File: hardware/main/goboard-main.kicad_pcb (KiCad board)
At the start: 2 copper layers, 312.7 x 138.4 mm, 152 parts, among them J1 USB_C_Receptacle_USB2.0, J2 Conn_02x05_Top_Bottom, J3 Conn_01x01, SW1 Esc, SW10 a, SW12 Fn, SW13 F2, SW14 2, SW15 w, SW16 s, SW17 z, SW18 Tux, SW19 F3, SW2 F1, SW20 3, SW21 e, SW22 d, SW23 c, SW24 Alt, SW25 F4, SW26 4, SW27 r, SW28 f, SW29 v, SW3 tilde, SW31 F5, SW32 5, SW33 t, SW34 g, SW35 b, SW36 F6, SW37 6, SW38 y, SW39 h, SW4 Tab, SW40 n, SW41 F7, SW42 7, SW43 u, SW44 j, SW45 m, SW46 Space, SW47 F8, SW48 8, SW49 i, SW5 Caps Lock, SW50 k, SW51 ,, SW52 F9, SW53 9, SW54 o, SW55 l, SW56 ., SW57 F10, SW58 0, SW59 p, SW6 Shift, SW60 ;, SW61 /, SW62 Alt Gr, SW63 F11, SW64 -, SW65 [, SW66 ', SW67 Menu, SW68 F12, SW69 =, SW7 Ctrl, SW70 ], SW71 \, SW72 Shift, SW73 Ctrl, SW74 Print, SW75 Backspace, SW76 Enter, SW77 Left, SW78 Scroll Lock, SW79 Up, SW8 1, SW80 Down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

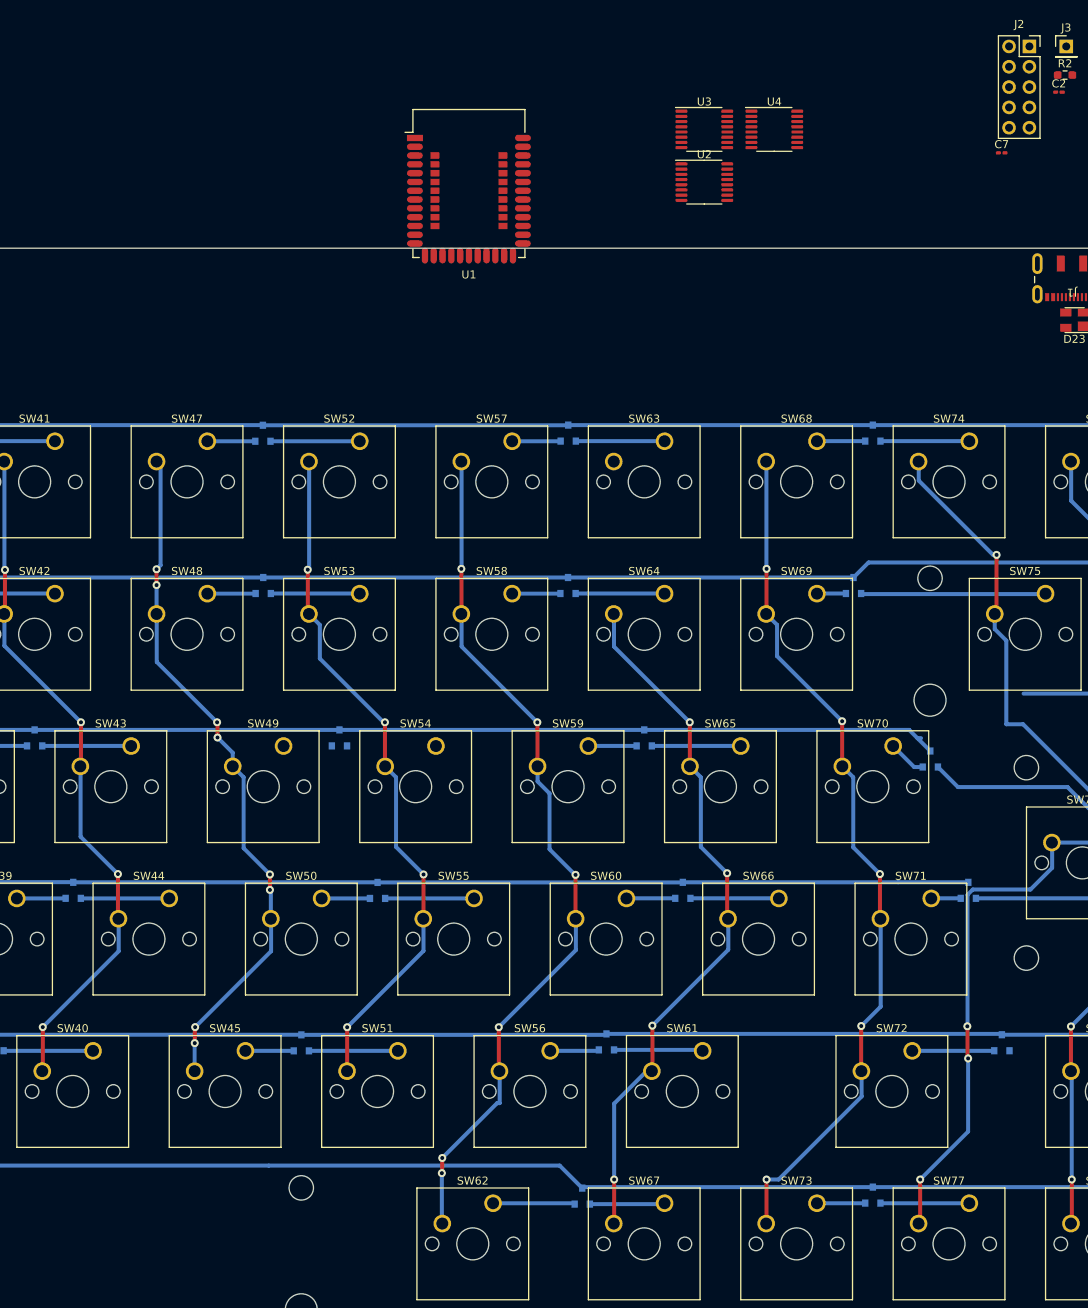
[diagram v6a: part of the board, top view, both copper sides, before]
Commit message: Add specialized connector for the programming port
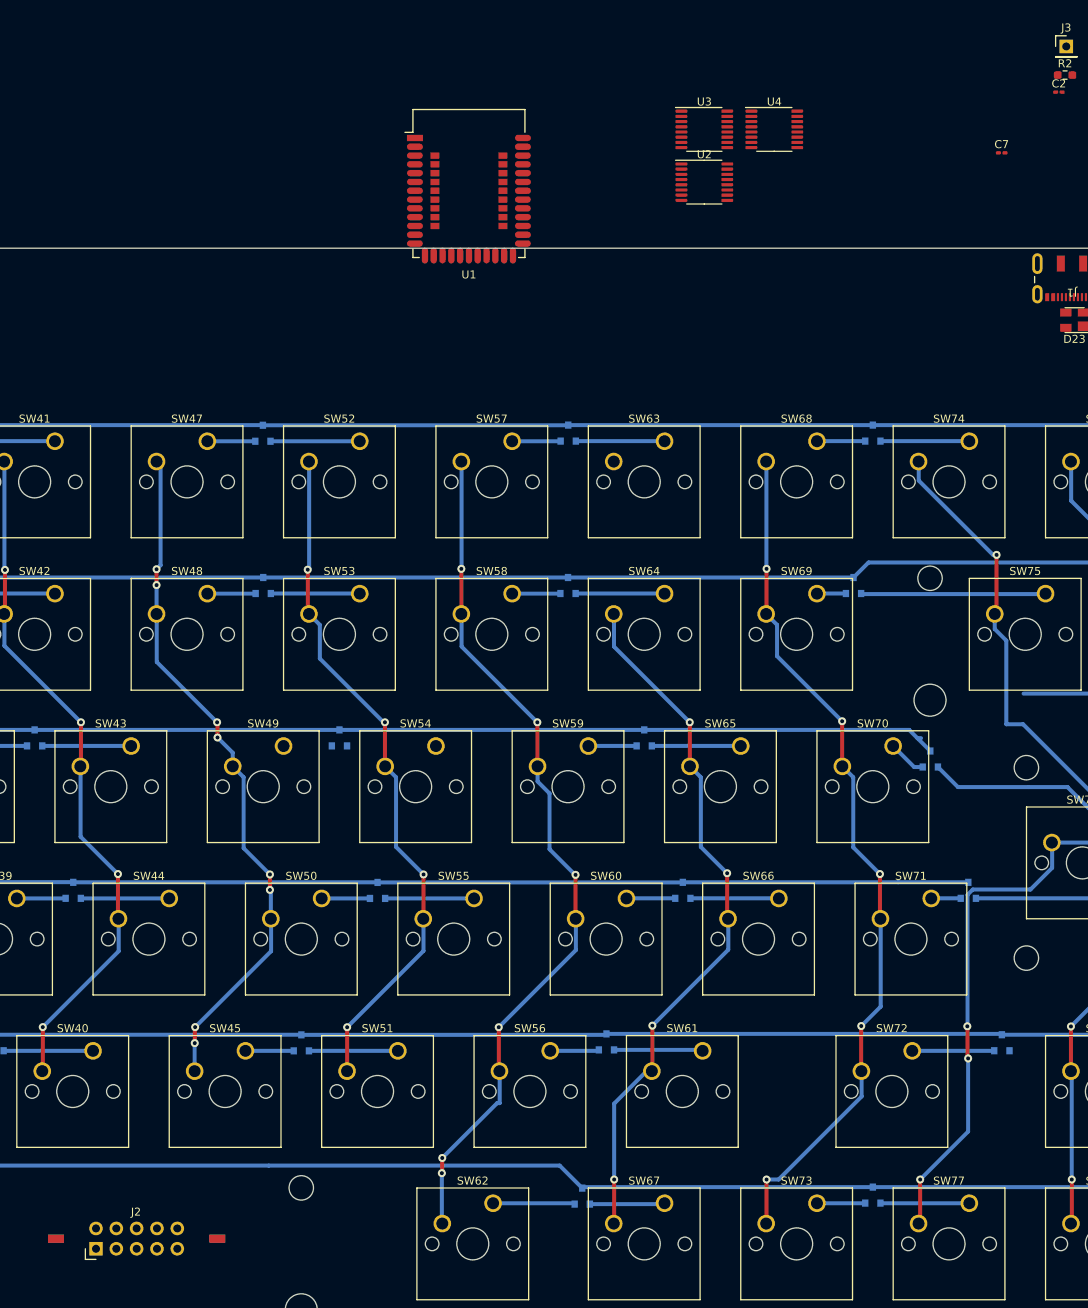
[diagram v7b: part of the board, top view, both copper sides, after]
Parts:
- J2: footprint Connector_PinSocket_2.54mm:PinSocket_2x05_P2.54mm_Vertical -> footprints:programming_port_st_link_clone
- moved J2 190.3 mm to (189.5, 174.7)
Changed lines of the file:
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@@
     )
   )
-  (footprint "Connector_PinSocket_2.54mm:PinSocket_2x05_P2.54mm_Vertical" (layer "F.Cu")
-    (at 306.1308 24.437)
-    (descr "Through hole straight socket strip, 2x05, 2.54mm pitch, double cols (from Kicad 4.0.7), script generated")
-    (tags "Through hole socket strip THT 2x05 2.54mm double row")
+  (footprint "footprints:programming_port_st_link_clone" (layer "F.Cu")
+    (at 189.4586 174.7266)
+    (descr "Through hole straight pin header, 2x05, 2.54mm pitch, double rows")
+    (tags "Through hole pin header THT 2x05 2.54mm double row")
     (property "Dateiname Blatt" "goboard-main.kicad_sch")
     (property "Schaltplanname" "")
     (attr through_hole)
-    (fp_text reference "J2" (at -1.27 -2.77) (layer "F.SilkS")
+    (fp_text reference "J2" (at 5 -4.6 180) (layer "F.SilkS")
       (effects (font (size 1 1) (thickness 0.15)))
     )
-    (fp_text value "Conn_02x05_Top_Bottom" (at -1.27 12.93) (layer "F.Fab")
+    (fp_text value "Conn_02x05_Top_Bottom" (at 5.1 2.1) (layer "F.Fab")
       (effects (font (size 1 1) (thickness 0.15)))
     )
-    (fp_text user "${REFERENCE}" (at -1.27 5.08 90) (layer "F.Fab")
+    (fp_text user "${REFERENCE}" (at 5.08 -1.27 180) (layer "F.Fab")
       (effects (font (size 1 1) (thickness 0.15)))
     )
-    (fp_line (start 0 -1.33) (end 1.33 -1.33) (layer "F.SilkS") (width 0.12))
-    (fp_line (start 1.33 -1.33) (end 1.33 0) (layer "F.SilkS") (width 0.12))
-    (fp_line (start -3.87 -1.33) (end -1.27 -1.33) (layer "F.SilkS") (width 0.12))
-    (fp_line (start 1.33 1.27) (end 1.33 11.49) (layer "F.SilkS") (width 0.12))
-    (fp_line (start -1.27 1.27) (end 1.33 1.27) (layer "F.SilkS") (width 0.12))
-    (fp_line (start -3.87 -1.33) (end -3.87 11.49) (layer "F.SilkS") (width 0.12))
-    (fp_line (start -1.27 -1.33) (end -1.27 1.27) (layer "F.SilkS") (width 0.12))
-    (fp_line (start -3.87 11.49) (end 1.33 11.49) (layer "F.SilkS") (width 0.12))
-    (fp_line (start 1.76 11.9) (end -4.34 11.9) (layer "F.CrtYd") (width 0.05))
-    (fp_line (start 1.76 -1.8) (end 1.76 11.9) (layer "F.CrtYd") (width 0.05))
-    (fp_line (start -4.34 11.9) (end -4.34 -1.8) (layer "F.CrtYd") (width 0.05))
-    (fp_line (start -4.34 -1.8) (end 1.76 -1.8) (layer "F.CrtYd") (width 0.05))
-    (fp_line (start -3.81 -1.27) (end 0.27 -1.27) (layer "F.Fab") (width 0.1))
-    (fp_line (start 1.27 11.43) (end -3.81 11.43) (layer "F.Fab") (width 0.1))
-    (fp_line (start 1.27 -0.27) (end 1.27 11.43) (layer "F.Fab") (width 0.1))
-    (fp_line (start 0.27 -1.27) (end 1.27 -0.27) (layer "F.Fab") (width 0.1))
-    (fp_line (start -3.81 11.43) (end -3.81 -1.27) (layer "F.Fab") (width 0.1))
-    (pad "1" thru_hole rect (at 0 0) (size 1.7 1.7) (drill 1) (layers *.Cu *.Mask)
+    (fp_line (start -1.33 1.33) (end -1.33 0) (layer "F.SilkS") (width 0.12))
+    (fp_line (start 0 1.33) (end -1.33 1.33) (layer "F.SilkS") (width 0.12))
+    (fp_line (start -1.8 -4.35) (end -1.8 -2.5) (layer "F.CrtYd") (width 0.05))
+    (fp_line (start -1.8 0.05) (end -1.8 1.8) (layer "F.CrtYd") (width 0.05))
+    (fp_line (start -1.8 -2.5) (end -6.5 -2.5) (layer "F.CrtYd") (width 0.05))
+    (fp_line (start 16.65 -2.6) (end 11.95 -2.6) (layer "F.CrtYd") (width 0.05))
+    (fp_line (start -6.5 0.05) (end -1.8 0.05) (layer "F.CrtYd") (width 0.05))
+    (fp_line (start 16.65 -0.05) (end 16.65 -2.6) (layer "F.CrtYd") (width 0.05))
+    (fp_line (start 11.95 -4.35) (end -1.8 -4.35) (layer "F.CrtYd") (width 0.05))
+    (fp_line (start -6.5 -2.5) (end -6.5 0.05) (layer "F.CrtYd") (width 0.05))
+    (fp_line (start 11.95 -0.05) (end 16.65 -0.05) (layer "F.CrtYd") (width 0.05))
+    (fp_line (start 11.95 1.8) (end 11.95 -0.05) (layer "F.CrtYd") (width 0.05))
+    (fp_line (start -1.8 1.8) (end 11.95 1.8) (layer "F.CrtYd") (width 0.05))
+    (fp_line (start 11.95 -2.6) (end 11.95 -4.35) (layer "F.CrtYd") (width 0.05))
+    (pad "" smd rect (at 15.16 -1.27 270) (size 1 2) (layers "F.Cu" "F.Paste" "F.Mask"))
+    (pad "" smd rect (at -5 -1.27 90) (size 1 2) (layers "B.Cu" "B.Paste" "B.Mask"))
+    (pad "" np_thru_hole oval (at 12.83 -1.27 270) (size 1 2.5) (drill oval 1 2.5) (layers F&B.Cu *.Mask))
+    (pad "" np_thru_hole oval (at -2.67 -1.27 90) (size 1 2.5) (drill oval 1 2.5) (layers F&B.Cu *.Mask))
+    (pad "" smd rect (at 15.16 -1.27 270) (size 1 2) (layers "B.Cu" "B.Paste" "B.Mask"))
+    (pad "" smd rect (at -5 -1.27 270) (size 1 2) (layers "F.Cu" "F.Paste" "F.Mask"))
+    (pad "1" thru_hole rect (at 0 0 90) (size 1.7 1.7) (drill 1) (layers *.Cu *.Mask)
       (net 37 "/RESET") (pinfunction "Pin_1"))
-    (pad "2" thru_hole oval (at -2.54 0) (size 1.7 1.7) (drill 1) (layers *.Cu *.Mask)
+    (pad "2" thru_hole oval (at 0 -2.54 90) (size 1.7 1.7) (drill 1) (layers *.Cu *.Mask)
       (net 47 "GND") (pinfunction "Pin_2"))
-    (pad "3" thru_hole oval (at 0 2.54) (size 1.7 1.7) (drill 1) (layers *.Cu *.Mask)
+    (pad "3" thru_hole oval (at 2.54 0 90) (size 1.7 1.7) (drill 1) (layers *.Cu *.Mask)
       (net 132 "no_connect_143") (pinfunction "Pin_3"))
-    (pad "4" thru_hole oval (at -2.54 2.54) (size 1.7 1.7) (drill 1) (layers *.Cu *.Mask)
+    (pad "4" thru_hole oval (at 2.54 -2.54 90) (size 1.7 1.7) (drill 1) (layers *.Cu *.Mask)
       (net 31 "VCC") (pinfunction "Pin_4"))
-    (pad "5" thru_hole oval (at 0 5.08) (size 1.7 1.7) (drill 1) (layers *.Cu *.Mask)
+    (pad "5" thru_hole oval (at 5.08 0 90) (size 1.7 1.7) (drill 1) (layers *.Cu *.Mask)
       (net 131 "no_connect_144") (pinfunction "Pin_5"))
-    (pad "6" thru_hole oval (at -2.54 5.08) (size 1.7 1.7) (drill 1) (layers *.Cu *.Mask)
+    (pad "6" thru_hole oval (at 5.08 -2.54 90) (size 1.7 1.7) (drill 1) (layers *.Cu *.Mask)
       (net 130 "/SWDIO") (pinfunction "Pin_6"))
-    (pad "7" thru_hole oval (at 0 7.62) (size 1.7 1.7) (drill 1) (layers *.Cu *.Mask)
+    (pad "7" thru_hole oval (at 7.62 0 90) (size 1.7 1.7) (drill 1) (layers *.Cu *.Mask)
       (net 47 "GND") (pinfunction "Pin_7"))
-    (pad "8" thru_hole oval (at -2.54 7.62) (size 1.7 1.7) (drill 1) (layers *.Cu *.Mask)
+    (pad "8" thru_hole oval (at 7.62 -2.54 90) (size 1.7 1.7) (drill 1) (layers *.Cu *.Mask)
       (net 129 "/SWDCLK") (pinfunction "Pin_8"))
-    (pad "9" thru_hole oval (at 0 10.16) (size 1.7 1.7) (drill 1) (layers *.Cu *.Mask)
+    (pad "9" thru_hole oval (at 10.16 0 90) (size 1.7 1.7) (drill 1) (layers *.Cu *.Mask)
       (net 31 "VCC") (pinfunction "Pin_9"))
-    (pad "10" thru_hole oval (at -2.54 10.16) (size 1.7 1.7) (drill 1) (layers *.Cu *.Mask)
+    (pad "10" thru_hole oval (at 10.16 -2.54 90) (size 1.7 1.7) (drill 1) (layers *.Cu *.Mask)
       (net 128 "no_connect_142") (pinfunction "Pin_10"))
-    (model "${KISYS3DMOD}/Connector_PinSocket_2.54mm.3dshapes/PinSocket_2x05_P2.54mm_Vertical.wrl"
-      (offset (xyz 0 0 0))
-      (scale (xyz 1 1 1))
-      (rotate (xyz 0 0 0))
-    )
   )
   (footprint "footprints:SW_Cherry_MX_1.75u_PCB" (layer "F.Cu")

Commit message: Adapt the layout for another keycap set
The layout is now compatible with this keycap set:
https://hk-gaming.com/collections/keycaps/products/hk-gaming-dye-
sublimation-cherry-profile-thick-pbt-keysets-for-mechanical-keyboard-139
-keys-chalk
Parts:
- removed SW67: Menu, footprints:SW_Cherry_MX_1.00u_PCB
- SW24: footprint footprints:SW_Cherry_MX_1.00u_PCB -> footprints:SW_Cherry_MX_1.25u_PCB
- SW62: footprint footprints:SW_Cherry_MX_1.25u_PCB -> footprints:SW_Cherry_MX_1.50u_PCB
- SW73: footprint footprints:SW_Cherry_MX_1.00u_PCB -> footprints:SW_Cherry_MX_1.50u_PCB
- moved D12 6.74 mm to (107.2, 167.7)
- moved SW62 6.63 mm to (245.3, 171.4)
- moved SW73 6.22 mm to (273.8, 171.4)
- moved SW46 4.49 mm to (171.4, 171.4)
- moved SW24 2.79 mm to (100.0, 171.4)
- moved D32 2.60 mm to (261.8, 132.3)
- moved D38 2.60 mm to (297.5, 132.3)
- moved SW72 2.60 mm to (290.5, 152.4)
- moved C2 2.60 mm to (308.8, 32.6)
- moved C1 2.60 mm to (317.8, 25.4)
- moved D45 2.60 mm to (335.8, 28.4)
- moved D47 2.60 mm to (335.8, 25.8)
- moved D10 2.60 mm to (106.7, 132.4)
- moved D14 2.60 mm to (133.2, 94.1)
- moved D15 2.60 mm to (142.7, 113.3)
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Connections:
- D40 pad 1: Net-(D40-Pad1) -> no_connect_140
- J1 pad A8: no_connect_140 -> no_connect_141
- J1 pad B8: no_connect_141 -> no_connect_142
- J2 pad 10: no_connect_142 -> no_connect_143
- J2 pad 3: no_connect_143 -> no_connect_144
- J2 pad 5: no_connect_144 -> no_connect_145
- SW73 pad 1: Net-(D40-Pad2) -> Net-(D34-Pad1)
- SW73 pad 2: Net-(SW68-Pad2) -> Net-(SW61-Pad2)
- SW77 pad 1: Net-(D40-Pad1) -> Net-(D40-Pad2)
- SW77 pad 2: Net-(SW74-Pad2) -> Net-(SW68-Pad2)
- U1 pad 10: no_connect_145 -> no_connect_146
- U1 pad 11: no_connect_146 -> no_connect_147
- U1 pad 18: no_connect_147 -> no_connect_148
- U1 pad 19: no_connect_148 -> no_connect_149
- U1 pad 2: no_connect_149 -> no_connect_150
- U1 pad 20: no_connect_150 -> /UART_TX
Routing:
- net Net-(SW74-Pad2): track 125.2 -> 66.4 mm, vias 4 -> 1
- net Net-(D40-Pad1): track 11.1 -> 0.00 mm
- net Net-(D34-Pad2): track 10.2 -> 3.10 mm
- net Net-(D40-Pad2): track 6.04 -> 10.8 mm
- net Net-(D12-Pad2): track 3.25 -> 7.32 mm
- net Net-(SW56-Pad2): track 108.6 -> 105.4 mm, vias 6 -> 5
- net Net-(SW68-Pad2): track 108.1 -> 105.2 mm
- net Net-(D12-Pad1): track 68.0 -> 65.4 mm
- net Net-(D34-Pad1): track 9.38 -> 11.1 mm
- net Net-(SW61-Pad2): track 88.4 -> 90.0 mm
- net Net-(SW13-Pad2): track 110.2 -> 111.2 mm, vias 10 -> 9
- net Net-(SW35-Pad2): vias 10 -> 9
